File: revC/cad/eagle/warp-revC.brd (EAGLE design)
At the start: 38.1 x 38.1 mm, 143 parts, among them J2 QIIC connector, J3 QIIC connector, J4 DF40FC-20DP-0.4V(51), J5 CORTEX_DEBUG_SMD, U1 MAX40200, U2 MAX40200

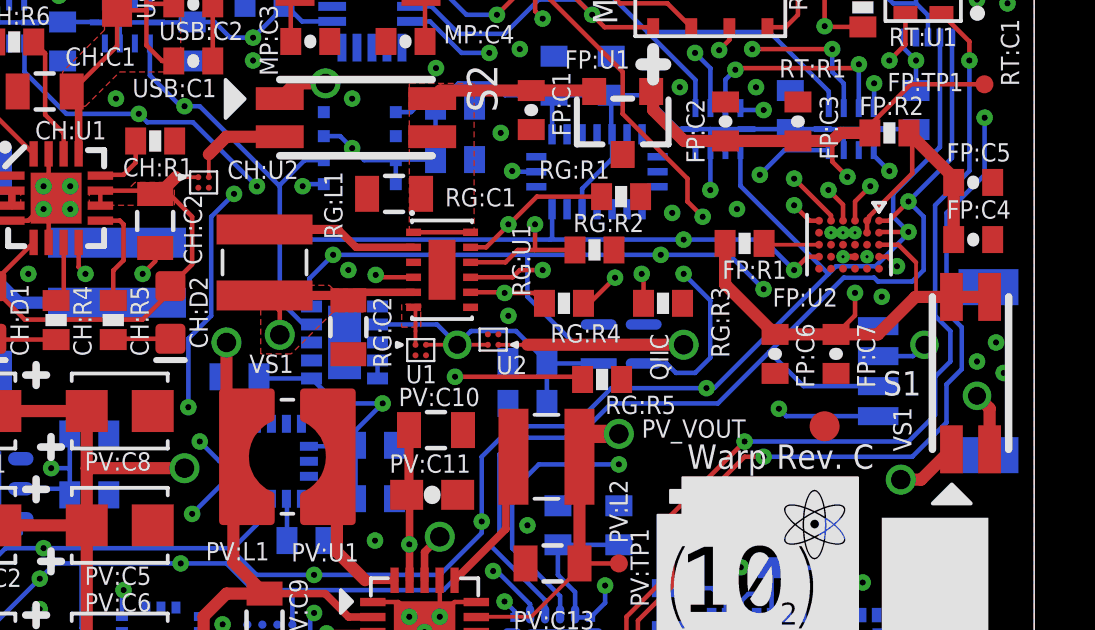
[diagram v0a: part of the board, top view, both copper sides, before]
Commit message: Removed FPGA microvias and rerouted
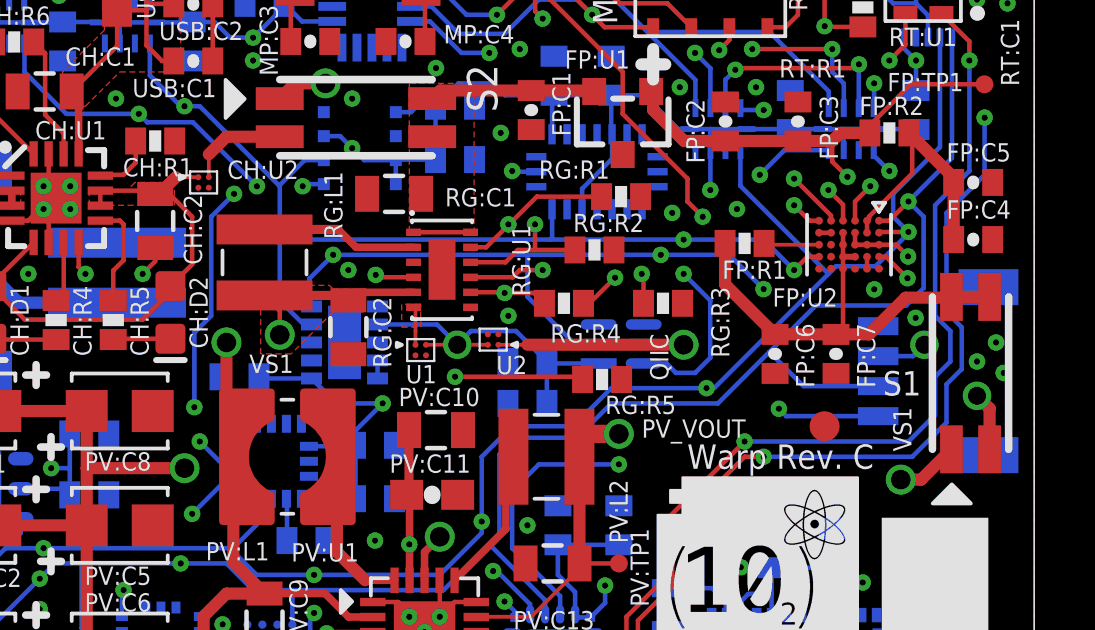
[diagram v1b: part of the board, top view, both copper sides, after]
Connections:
- net FP:VCC_1V2: now also FP:U2.A3, FP:U2.B3, FP:U2.C3
- net FPGA_VS: now also FP:U2.D3, FP:U2.D5; no longer FP:U2.A3
- net GND: now also FP:U2.B5, FP:U2.F2
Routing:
- net FP:VCC_1V2: track 16.5 -> 20.3 mm
- net FPGA_VS: track 18.2 -> 15.3 mm, vias 3 -> 0
- net GND: track 51.4 -> 50.6 mm, vias 80 -> 79
- net I2C1_SCL: track 96.6 -> 97.1 mm

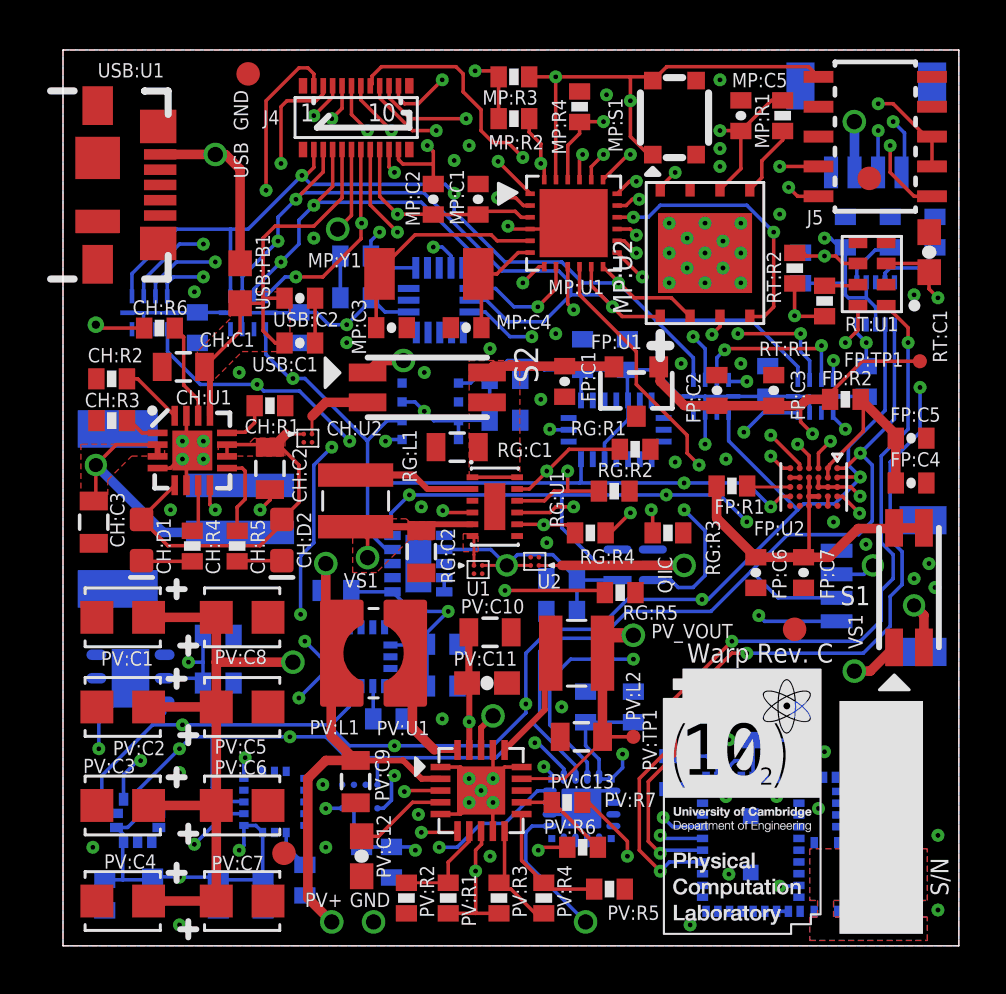
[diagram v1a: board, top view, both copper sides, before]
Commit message: MAG3110 with FXOS8700CQ. Added BOM
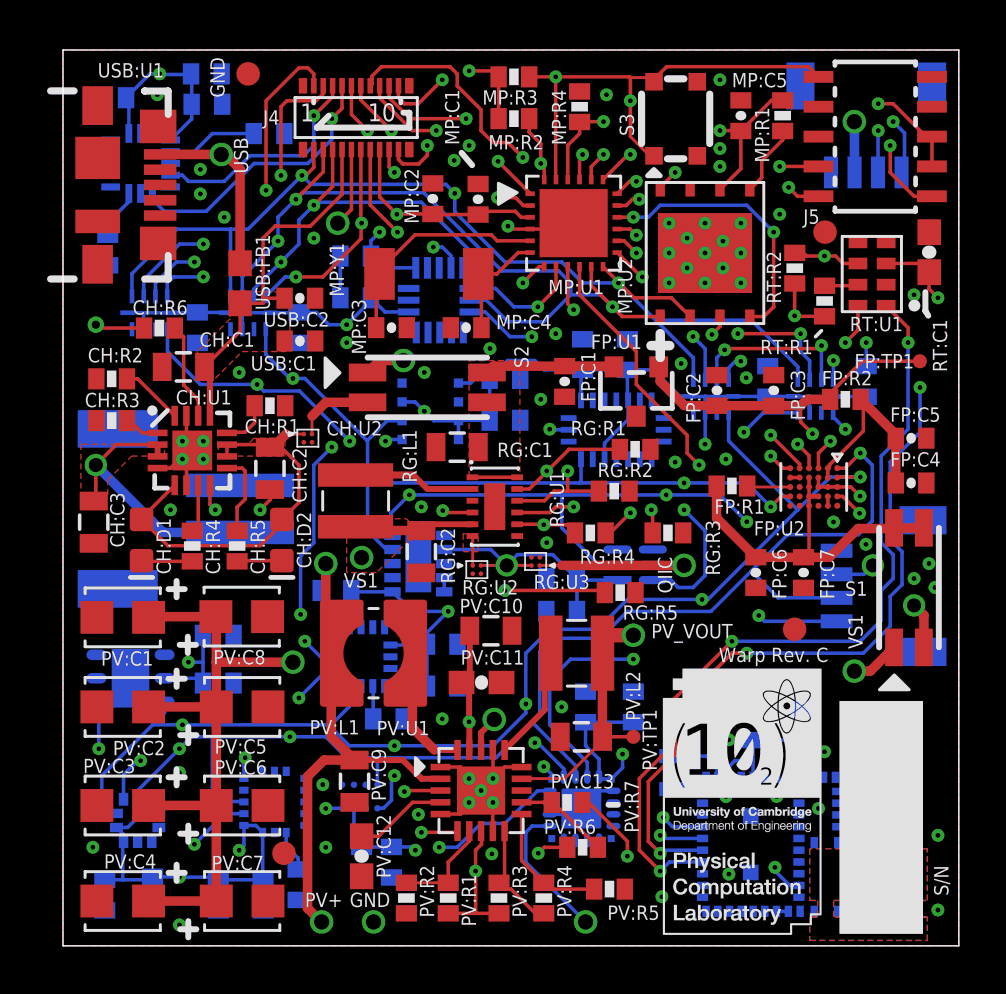
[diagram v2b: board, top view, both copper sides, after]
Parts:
- removed MP:S1: EVPAYG0BAEVPAYG0BA, EVPAYG0BA:EVPAYG0BA
- removed U1, U2: MAX40200, MAX40200:DSBGA
- added RG:U2, RG:U3: MAX40200, MAX40200:DSBGA
- added S3: EVPAYG0BAEVPAYG0BA, EVPAYG0BA:EVPAYG0BA
- added SB:C19: 0.1uF, SparkFun-Passives:0402-CAP
- CH:D1: value (none) -> Green
- CH:D2: value (none) -> Red
- CH:R4, CH:R5: value 4.7k -> 2k
- MP:C2, USB:C1: value 4.7uF (pol) -> 4.7uF
- SB:C10: value 1uF -> 4.7uF
- SB:C6: value 10nF (25V) -> 10nF
- SB:U4: value MAG3110 -> FXOS8700CQ; device MAG3110:MAG3110 -> FXOS8700CQ:QFN16
- moved SB:C12 33.3 mm to (1.91, 29.6), turned to 270 degrees
- moved SB:U4 31.8 mm to (3.30, 33.3), turned to 0 degrees
- moved SB:C11 28.6 mm to (8.76, 34.5), turned to 180 degrees
- moved SB:C9 27.7 mm to (6.12, 35.8), turned to 180 degrees
- moved SB:C10 26.6 mm to (6.10, 37.1), turned to 180 degrees
- moved FD2 2.96 mm to (32.4, 30.4)
- moved SB:C6 0.35 mm to (10.0, 2.60)
- moved PV:C11 0.24 mm to (17.8, 11.2)
- moved USB:C1 0.09 mm to (10.1, 25.7)
- moved PV:C10 0.08 mm to (18.2, 13.4)
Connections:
- removed net REG_LOAD: RG:U1.6, U1.A1
- removed net SB:N$17: SB:C12.1, SB:U4.P$1
- new net RG:LOAD: RG:U1.6, RG:U2.A1
- new net SB:N$3: SB:C12.1, SB:U4.8
- net GND: now also RG:U2.B2, RG:U3.B2, S3.B, S3.B', SB:C19.2, SB:U4.10, SB:U4.12, SB:U4.13, SB:U4.16, SB:U4.3, SB:U4.5, SB:U4.7; no longer MP:S1.B, MP:S1.B', SB:U4.P$10, SB:U4.P$5, U1.B2, U2.B2
- net I2C2_SCL: now also SB:U4.4; no longer SB:U4.P$7
- net I2C2_SDA: now also SB:U4.6; no longer SB:U4.P$6
- net RTC_!INT!/RESET_B: now also S3.A, S3.A'; no longer MP:S1.A, MP:S1.A'
- net SB:N$2: now also SB:U4.2; no longer SB:U4.P$4
- net VCC_QIIC: now also RG:U3.A1; no longer U2.A1
- net VS2: now also RG:U2.A2, RG:U3.A2, SB:C19.1, SB:U4.1, SB:U4.14; no longer SB:U4.P$2, SB:U4.P$8, U1.A2, U2.A2
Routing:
- net GND: track 50.6 -> 46.4 mm, vias 79 -> 82
- net I2C2_SDA: track 114.4 -> 118.6 mm
- net SB:N$17: track 2.44 -> 0.00 mm
- net USB_5V: track 18.6 -> 16.2 mm
- net SB:N$3: track 0.00 -> 2.13 mm
- net REG_LOAD: track 1.28 -> 0.00 mm
- net RG:LOAD: track 0.00 -> 1.26 mm
- net VS1: track 36.7 -> 35.5 mm
- net SB:N$2: track 3.11 -> 3.85 mm
- net ISL23415_SPI_CS: track 48.7 -> 49.4 mm
- net I2C2_SCL: track 124.0 -> 124.6 mm

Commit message: Corrected footprint errors
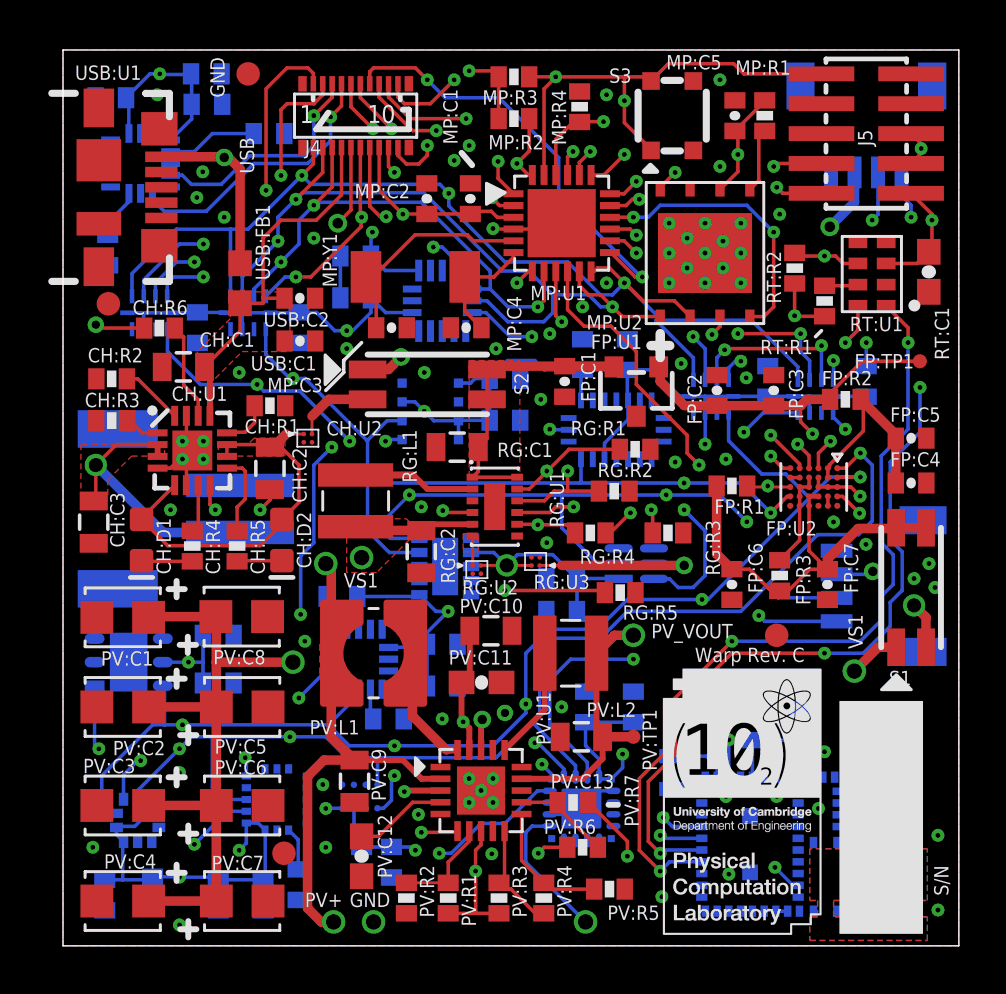
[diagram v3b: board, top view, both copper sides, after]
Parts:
- added FP:R3: 10k, SparkFun-Passives:0402-RES
- J5: value CORTEX_DEBUG_SMD -> CORTEX_DEBUGCORTEX_DEBUG; device SparkFun-Connectors:SAMTECH_FTSH-105-01 -> CORTEX_DEBUG:10PIN
- moved FD2 30.6 mm to (1.93, 27.3)
- moved BT:U1 4.01 mm to (32.9, 1.47)
- moved S3 2.54 mm to (25.9, 35.3)
- moved J4 2.18 mm to (12.4, 35.3)
- moved MP:Y1 1.53 mm to (15.0, 28.4)
- moved S2 1.40 mm to (15.5, 23.9)
- moved S1 1.18 mm to (36.1, 15.2)
- moved SA:U3 1.15 mm to (16.3, 16.1), turned to 270 degrees
- moved FP:C7 1.14 mm to (32.5, 15.4)
- moved FP:C6 1.14 mm to (28.4, 15.4)
- moved RT:C1 0.84 mm to (36.8, 28.7), turned to 270 degrees
- moved FD3 0.80 mm to (30.4, 13.2)
- moved MP:R1 0.76 mm to (29.8, 35.3)
- moved SB:U3 0.65 mm to (2.79, 12.1), turned to 90 degrees
- moved MP:U1 0.51 mm to (21.2, 30.7)
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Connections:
- removed net FP:CRESET_B: FP:R1.1, FP:U2.F3
- new net CRESET_B: FP:R1.1, FP:U2.F3, J4.P$17
- new net FP:VCC_SHUNT: FP:R3.1, FP:U2.D2, FP:U2.D3, FP:U2.E3, FP:U2.E4, FP:U2.E5
- net BGX13S_!RST: no longer J4.P$7
- net FPGA_CS: now also J4.P$7
- net FPGA_VS: now also FP:R3.2; no longer FP:U2.D2, FP:U2.D3
- net GND: now also SA:U5.3, SB:U1.10, SB:U1.12, SB:U1.5, SB:U1.7, SB:U2.10, SB:U2.11, SB:U2.12, SB:U2.13, SB:U2.15, SB:U2.4, SB:U2.9, SB:U3.2, SB:U5.3, SB:U5.5, SB:U5.8, SB:U5.9; no longer SA:U5.P$3, SB:U1.P$10, SB:U1.P$12, SB:U1.P$5, SB:U1.P$7, SB:U2.P$10, SB:U2.P$11, SB:U2.P$12, SB:U2.P$13, SB:U2.P$15, SB:U2.P$4, SB:U2.P$9, SB:U3.P$2, SB:U5.P$3, SB:U5.P$5, SB:U5.P$8, SB:U5.P$9
- net I2C1_SCL: now also SA:U5.2; no longer SA:U5.P$2
- net I2C1_SDA: now also SA:U5.6; no longer SA:U5.P$6
- net I2C2_SCL: now also SB:U1.4, SB:U2.2, SB:U3.6, SB:U5.2; no longer SB:U1.P$4, SB:U2.P$2, SB:U3.P$6, SB:U5.P$2
- net I2C2_SDA: now also SB:U1.6, SB:U2.3, SB:U3.1, SB:U5.4; no longer SB:U1.P$6, SB:U2.P$3, SB:U3.P$1, SB:U5.P$4
- net SB:CAP: now also SB:U2.14; no longer SB:U2.P$14
- net SB:N$1: now also SB:U1.2; no longer SB:U1.P$2
- net SI4705_!RST: no longer J4.P$17
- net VS2: now also SA:U5.1, SB:U1.1, SB:U1.14, SB:U2.1, SB:U2.16, SB:U2.5, SB:U3.5, SB:U5.1, SB:U5.10, SB:U5.6; no longer SA:U5.P$1, SB:U1.P$1, SB:U1.P$14, SB:U2.P$1, SB:U2.P$16, SB:U2.P$5, SB:U3.P$5, SB:U5.P$1, SB:U5.P$10, SB:U5.P$6
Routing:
- net CRESET_B: track 0.00 -> 35.3 mm, vias 0 -> 4
- net FPGA_CS: track 15.2 -> 32.3 mm, vias 2 -> 3
- net BGX13S_!RST: track 47.9 -> 33.3 mm, vias 3 -> 2
- net GND: track 46.4 -> 31.9 mm, vias 82 -> 81
- net REG_VIN: track 7.42 -> 12.2 mm
- net FP:VCC_SHUNT: track 0.00 -> 4.27 mm
- net VS1: track 35.5 -> 31.8 mm, vias 9 -> 8
- net VCC_QIIC: track 37.7 -> 34.5 mm
- net I2C1_SCL: track 97.1 -> 94.0 mm
- net FPGA_VS: track 15.3 -> 17.6 mm
- net FP:CRESET_B: track 1.85 -> 0.00 mm
- net I2C1_SDA: track 85.3 -> 83.5 mm
- net SI4705_!RST: track 51.6 -> 52.8 mm, vias 5 -> 4
- net REG_VSEL4: track 22.1 -> 23.0 mm
- net I2C2_SCL: track 124.6 -> 125.6 mm
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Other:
- board text removed: "QIIC"

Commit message: Corrections to footprints
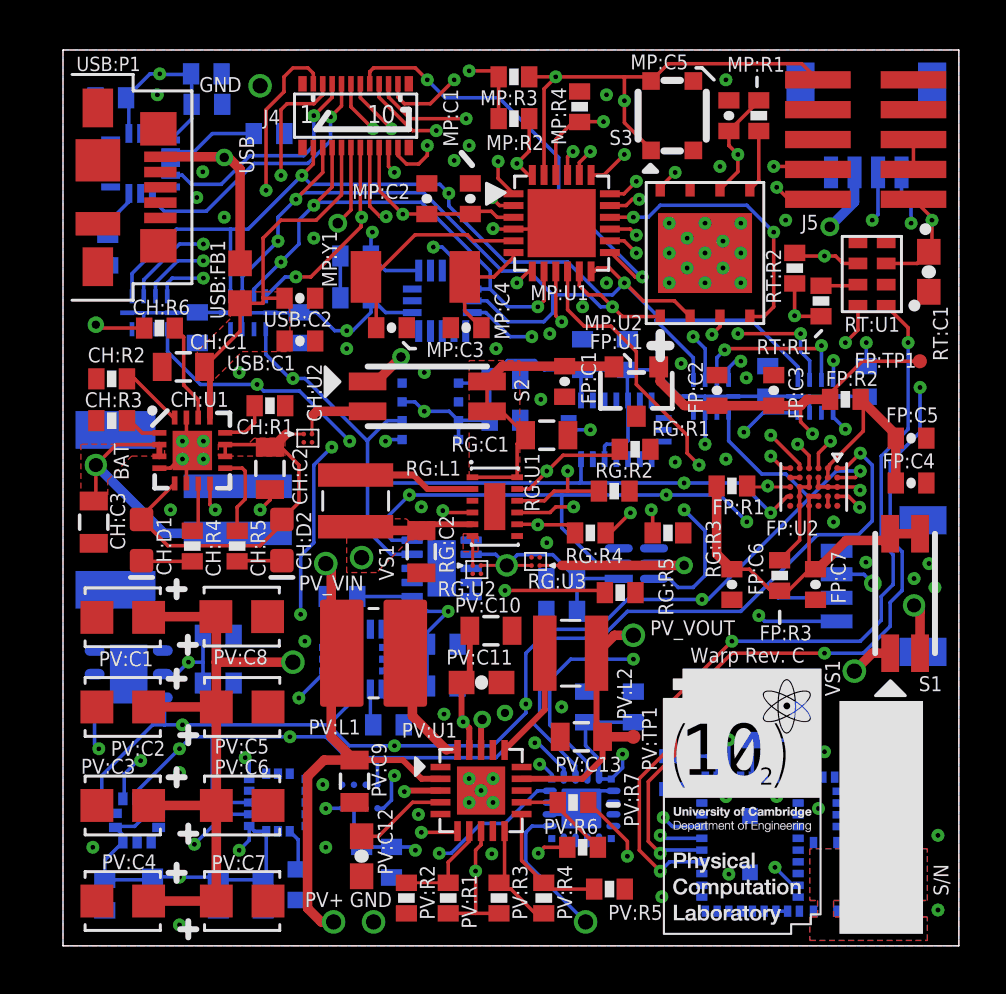
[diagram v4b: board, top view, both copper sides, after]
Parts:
- removed FD1, FD2, FD3, FD4: FIDUCIAL1X2, SparkFun-Aesthetics:FIDUCIAL-1X2
- removed USB:U1: MOLEX_USB_47346-0001MICRO_USB_B, MOLEX MICRO USB:USB-B-MICRO-SMD
- added USB:P1: MOLEX_USB_47346-0001MICRO_USB_B, MOLEX MICRO USB:USB-B-MICRO-SMD
- J5: value CORTEX_DEBUGCORTEX_DEBUG -> FTSH-105-01-XXX-DV-K; device CORTEX_DEBUG:10PIN -> FTSH-105-01-XXX-DV-K:FTSH-105-01-XXX-DV-K
- SA:U3: device SparkFun-Sensors:LGA10 -> CCS811:SON60P270X400X110-11N
- moved RG:C1 3.84 mm to (20.6, 21.7), turned to 0 degrees
- moved J1 1.30 mm to (5.13, 18.5)
- moved FP:C7 0.51 mm to (32.0, 15.4)
- moved S2 0.51 mm to (15.5, 23.4)
- moved SB:U3 0.51 mm to (2.79, 11.6), turned to 270 degrees
- moved S1 0.36 mm to (35.8, 15.0)
- moved J5 0.26 mm to (34.1, 34.3)
- moved SB:C3 0.25 mm to (13.8, 9.40)
- moved MP:C5 0.25 mm to (28.3, 35.3)
- moved MP:R1 0.25 mm to (29.6, 35.3)
- moved SA:U3 0.17 mm to (16.1, 16.1), turned to 90 degrees
- moved RT:R1 0.15 mm to (32.2, 27.4)
- moved SB:U2 0.13 mm to (9.14, 6.10), turned to 270 degrees
- moved SB:U7 0.05 mm to (12.6, 6.35), turned to 270 degrees
- turned SB:U5 to 180 degrees
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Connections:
- net SA:N$7 renamed SA:N$2
- net GND: now also SA:U3.11, SB:U4.P$10, SB:U4.P$12, SB:U4.P$13, SB:U4.P$16, SB:U4.P$3, SB:U4.P$5, SB:U4.P$7, USB:P1.5, USB:P1.S1, USB:P1.S2, USB:P1.S3, USB:P1.S4, USB:P1.S5, USB:P1.S6; no longer SA:U3.EP, SB:U4.10, SB:U4.12, SB:U4.13, SB:U4.16, SB:U4.3, SB:U4.5, SB:U4.7, USB:U1.GND, USB:U1.S1, USB:U1.S2, USB:U1.S3, USB:U1.S4, USB:U1.S5, USB:U1.S6
- net I2C2_SCL: now also SB:U4.P$4; no longer SB:U4.4
- net I2C2_SDA: now also SB:U4.P$6; no longer SB:U4.6
- net PV:LBUCK: now also PV:L2.2; no longer PV:L2.1
- net PV_VOUT: now also PV:L2.1; no longer PV:L2.2
- net SB:N$2: now also SB:U4.P$2; no longer SB:U4.2
- net SB:N$3: now also SB:U4.P$8; no longer SB:U4.8
- net USB:VBUS: now also USB:P1.1; no longer USB:U1.VBUS
- net VS2: now also SB:U4.P$1, SB:U4.P$14; no longer SB:U4.1, SB:U4.14
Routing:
- net I2C1_SCL: track 94.0 -> 91.9 mm
- net CRESET_B: track 35.3 -> 36.5 mm
- net VS2: track 125.4 -> 126.4 mm
- net VCC_QIIC: track 34.5 -> 35.4 mm
- net FPGA_VS: track 17.6 -> 16.8 mm
- net VS1: track 31.8 -> 31.1 mm
- net REG_VIN: track 12.2 -> 12.9 mm
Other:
- board text added: "BAT"
- board text added: "PV_VIN"

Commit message: Commit of CAD design, BOM and datasheets for 1st production run of Warp-revC
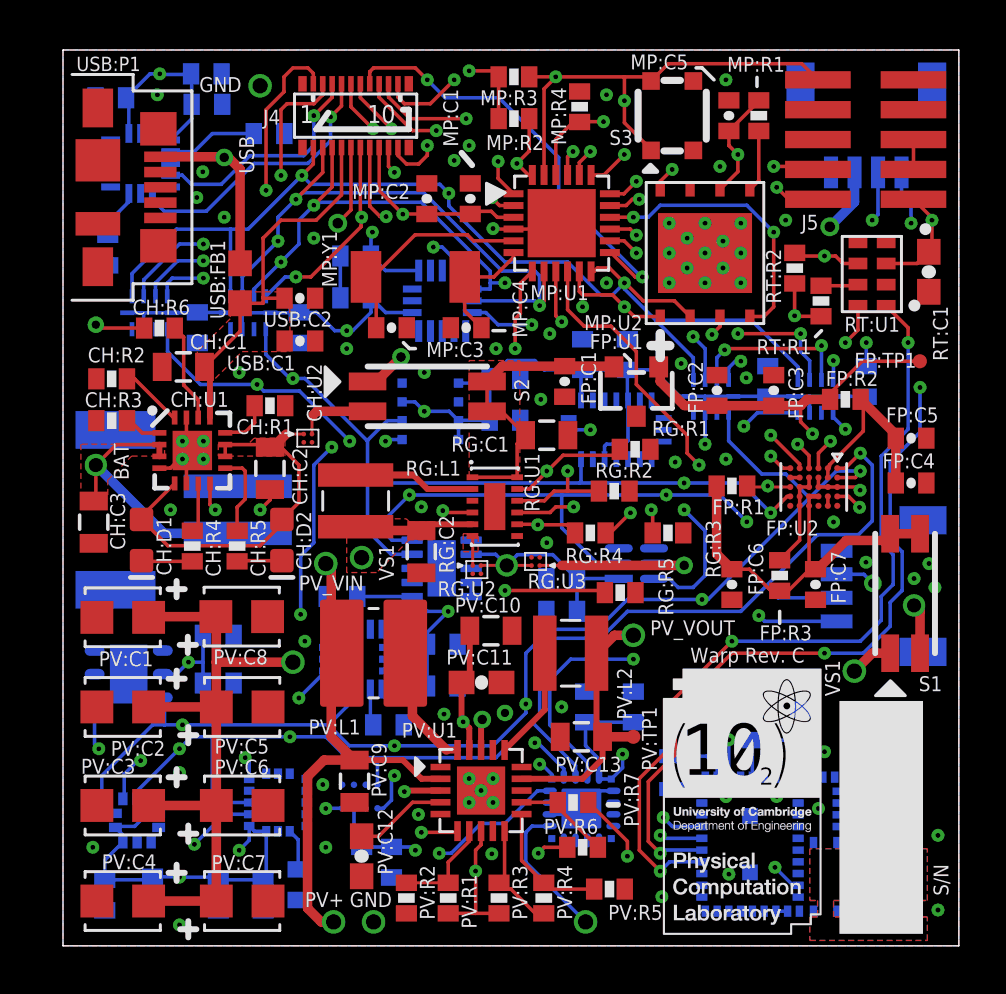
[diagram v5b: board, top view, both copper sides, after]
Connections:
- net SPI_MISO/UART_RTS: now also MP:U1.P$8, MP:U2.8; no longer MP:U1.P$11, MP:U2.1
- net SPI_MOSI/UART_CTS: now also MP:U1.P$11, MP:U2.1; no longer MP:U1.P$8, MP:U2.8
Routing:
- net SPI_MOSI/UART_CTS: track 98.4 -> 81.9 mm
- net CRESET_B: track 36.5 -> 28.8 mm
- net BGX13S_!RST: track 33.3 -> 32.5 mm
- net REG_CTRL: track 50.2 -> 49.5 mm
- net ADXL362_SPI_CS: track 10.6 -> 10.0 mm
- net ISL23415_SPI_CS: track 49.1 -> 49.6 mm
- net SPI_MISO/UART_RTS: track 90.2 -> 90.7 mm, vias 9 -> 10
